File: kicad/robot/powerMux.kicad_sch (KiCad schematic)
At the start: 8 parts, among them Q1 Q_NMOS_GDS, U4 NCP3901

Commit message: Assigned resistor footprints
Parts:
- R16, R17, R18: footprint (none) -> Resistor_SMD:R_0603_1608Metric
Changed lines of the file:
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@@
       (effects (font (size 1.27 1.27)) (justify left))
     )
-    (property "Footprint" "" (id 2) (at 172.212 123.19 90)
+    (property "Footprint" "Resistor_SMD:R_0603_1608Metric" (id 2) (at 172.212 123.19 90)
       (effects (font (size 1.27 1.27)) hide)
     )
@@
       (effects (font (size 1.27 1.27)) (justify left))
     )
-    (property "Footprint" "" (id 2) (at 207.772 67.31 90)
+    (property "Footprint" "Resistor_SMD:R_0603_1608Metric" (id 2) (at 207.772 67.31 90)
       (effects (font (size 1.27 1.27)) hide)
     )
@@
       (effects (font (size 1.27 1.27)) (justify left))
     )
-    (property "Footprint" "" (id 2) (at 172.212 135.89 90)
+    (property "Footprint" "Resistor_SMD:R_0603_1608Metric" (id 2) (at 172.212 135.89 90)
       (effects (font (size 1.27 1.27)) hide)
     )

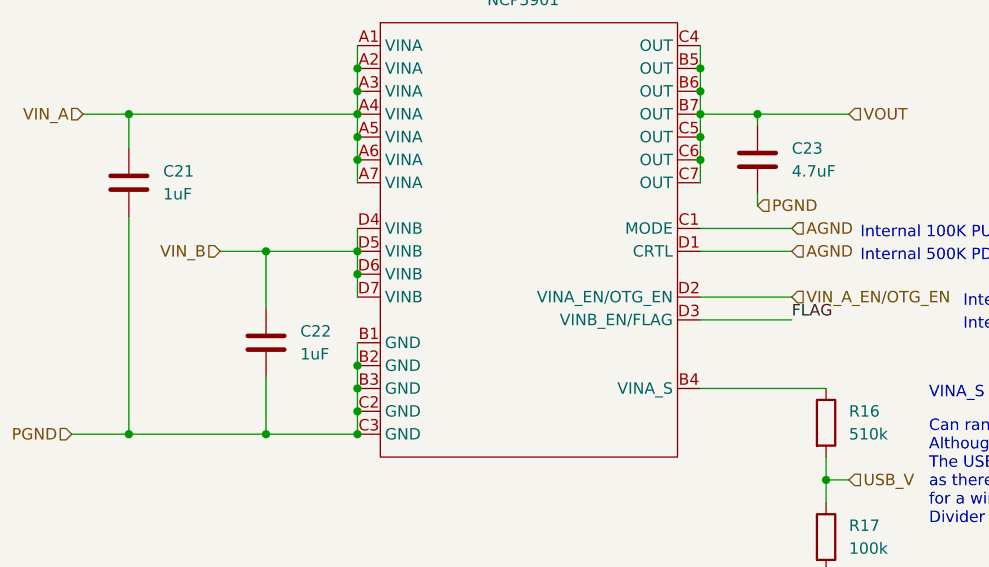
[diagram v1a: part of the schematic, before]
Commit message: Assigned capacitor footprints
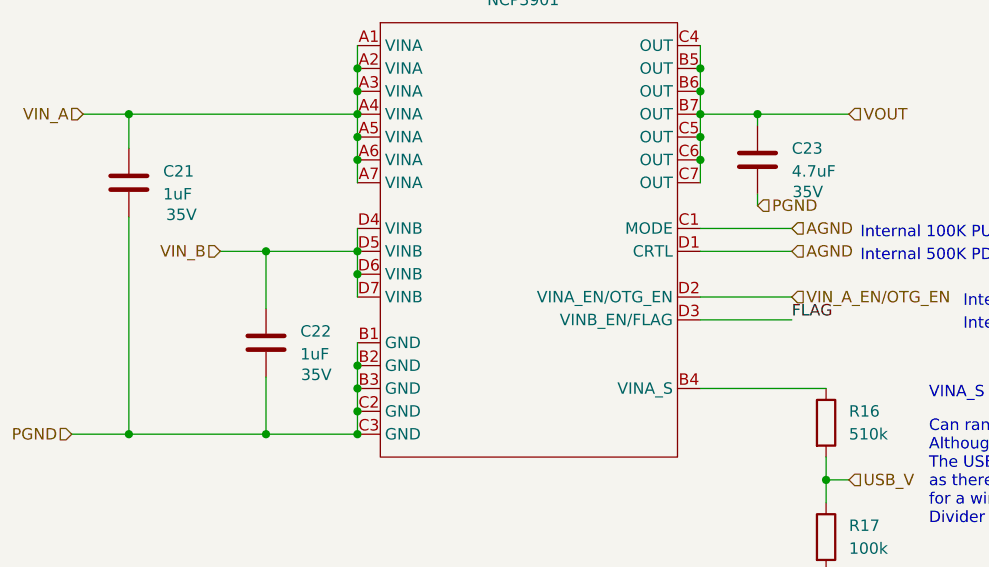
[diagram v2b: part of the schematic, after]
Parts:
- C21, C22, C23: footprint (none) -> Capacitor_SMD:C_0805_2012Metric
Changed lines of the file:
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@@
   )
   (symbol (lib_id "Device:C") (at 166.37 93.98 0) (unit 1)
-    (in_bom yes) (on_board yes) (fields_autoplaced)
+    (in_bom yes) (on_board yes)
     (property "Reference" "C23" (id 0) (at 170.18 92.7099 0)
       (effects (font (size 1.27 1.27)) (justify left))
@@
       (effects (font (size 1.27 1.27)) (justify left))
     )
-    (property "Footprint" "" (id 2) (at 167.3352 97.79 0)
+    (property "Footprint" "Capacitor_SMD:C_0805_2012Metric" (id 2) (at 167.3352 97.79 0)
       (effects (font (size 1.27 1.27)) hide)
     )
@@
       (effects (font (size 1.27 1.27)) hide)
     )
+    (property "Description" "35V" (id 4) (at 171.958 97.536 0))
     (pin "1")
     (pin "2")
@@
   )
   (symbol (lib_id "Device:C") (at 111.76 114.3 0) (unit 1)
-    (in_bom yes) (on_board yes) (fields_autoplaced)
+    (in_bom yes) (on_board yes)
     (property "Reference" "C22" (id 0) (at 115.57 113.0299 0)
       (effects (font (size 1.27 1.27)) (justify left))
@@
       (effects (font (size 1.27 1.27)) (justify left))
     )
-    (property "Footprint" "" (id 2) (at 112.7252 118.11 0)
+    (property "Footprint" "Capacitor_SMD:C_0805_2012Metric" (id 2) (at 112.7252 118.11 0)
       (effects (font (size 1.27 1.27)) hide)
     )
@@
       (effects (font (size 1.27 1.27)) hide)
     )
+    (property "Description" "35V" (id 4) (at 117.348 117.856 0))
     (pin "1")
     (pin "2")
@@
   )
   (symbol (lib_id "Device:C") (at 96.52 96.52 0) (unit 1)
-    (in_bom yes) (on_board yes) (fields_autoplaced)
+    (in_bom yes) (on_board yes)
     (property "Reference" "C21" (id 0) (at 100.33 95.2499 0)
       (effects (font (size 1.27 1.27)) (justify left))
@@
       (effects (font (size 1.27 1.27)) (justify left))
     )
-    (property "Footprint" "" (id 2) (at 97.4852 100.33 0)
+    (property "Footprint" "Capacitor_SMD:C_0805_2012Metric" (id 2) (at 97.4852 100.33 0)
       (effects (font (size 1.27 1.27)) hide)
     )
@@
       (effects (font (size 1.27 1.27)) hide)
     )
+    (property "Description" "35V" (id 4) (at 102.362 100.076 0))
     (pin "1")
     (pin "2")

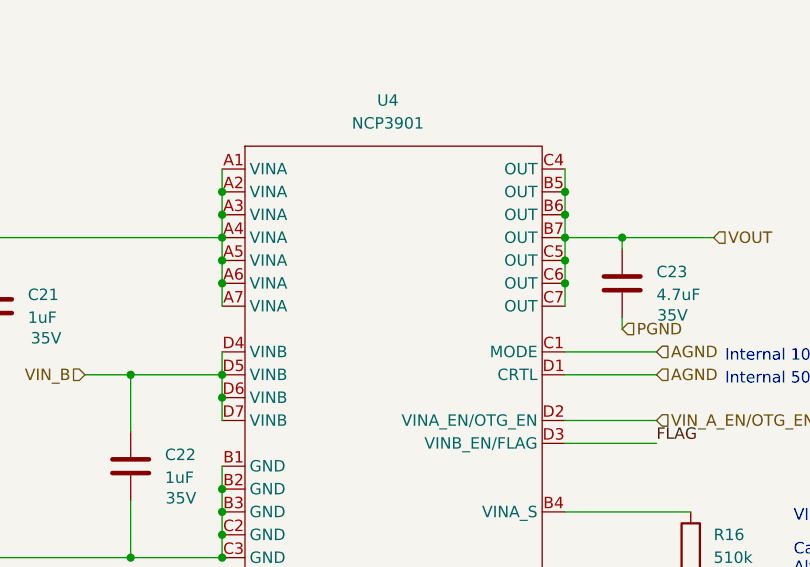
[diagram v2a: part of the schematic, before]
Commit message: Added footprint to NCP3901
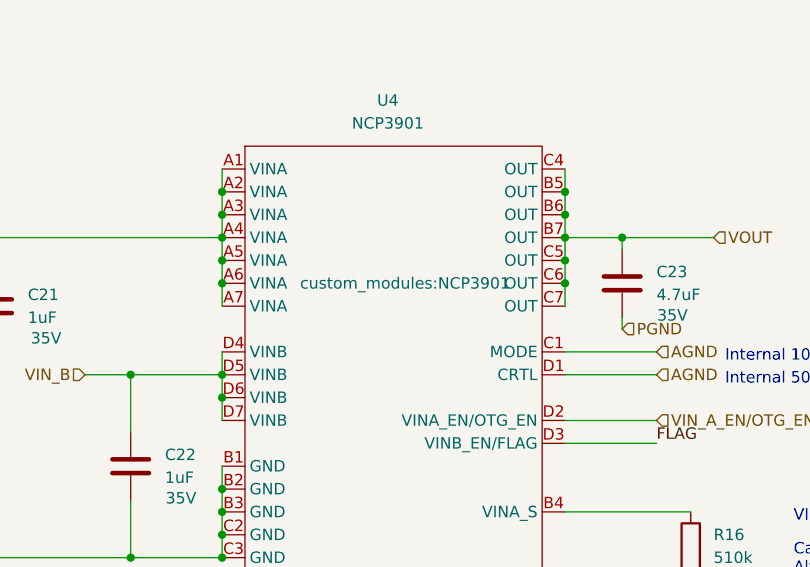
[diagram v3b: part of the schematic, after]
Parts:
- U4: footprint (none) -> custom_modules:NCP3901
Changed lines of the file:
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@@
     (property "Reference" "U4" (id 0) (at 140.335 73.66 0))
     (property "Value" "NCP3901" (id 1) (at 140.335 76.2 0))
-    (property "Footprint" "" (id 2) (at 142.24 93.98 0)
-      (effects (font (size 1.27 1.27)) hide)
-    )
+    (property "Footprint" "custom_modules:NCP3901" (id 2) (at 142.24 93.98 0))
     (property "Datasheet" "https://www.onsemi.com/pdf/datasheet/ncp3901-d.pdf" (id 3) (at 142.24 93.98 0)
       (effects (font (size 1.27 1.27)) hide)

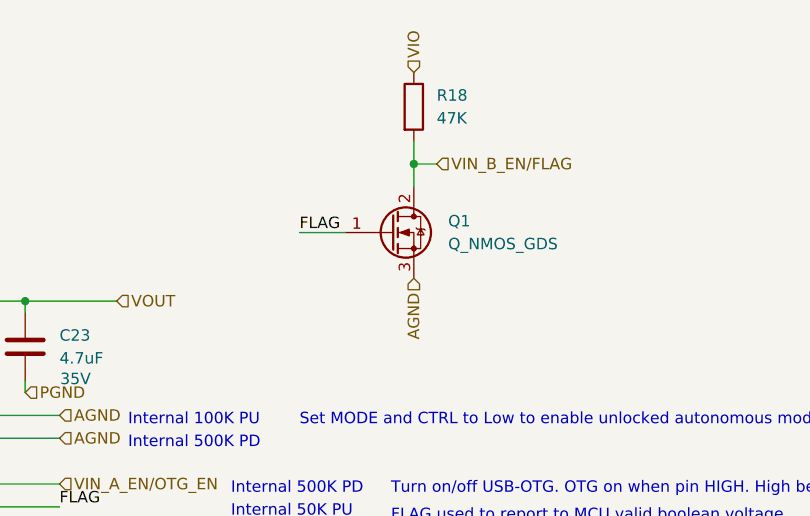
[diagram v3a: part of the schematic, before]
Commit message: Added part and footprint for mux mosfet.
Swapped pins 2 and 3 to match part.
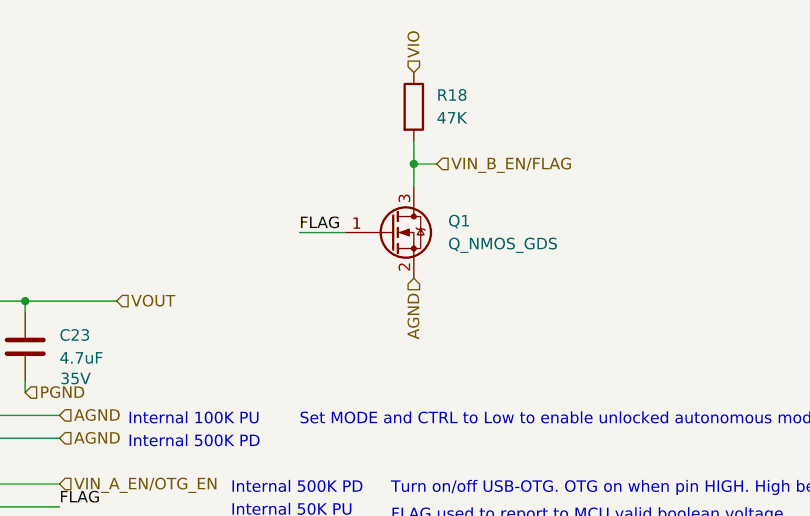
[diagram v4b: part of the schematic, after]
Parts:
- Q1: footprint (none) -> Package_TO_SOT_SMD:SOT-23; symbol Device:Q_NMOS_GDS -> Device:Q_NMOS_GSD; Part Number (none) -> T2N7002AK,LM
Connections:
- net AGND: now also Q1.2 (S); no longer Q1.3 (S)
- net VIN_B_EN/FLAG: now also Q1.3 (D); no longer Q1.2 (D)
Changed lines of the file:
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@@
     (pin "2")
   )
-  (symbol (lib_id "Device:Q_NMOS_GDS") (at 207.01 81.28 0) (unit 1)
+  (symbol (lib_id "Device:Q_NMOS_GSD") (at 207.01 81.28 0) (unit 1)
     (in_bom yes) (on_board yes) (fields_autoplaced)
     (property "Reference" "Q1" (id 0) (at 213.36 80.0099 0)
@@
       (effects (font (size 1.27 1.27)) (justify left))
     )
-    (property "Footprint" "" (id 2) (at 212.09 78.74 0)
+    (property "Footprint" "Package_TO_SOT_SMD:SOT-23" (id 2) (at 212.09 78.74 0)
       (effects (font (size 1.27 1.27)) hide)
     )
@@
       (effects (font (size 1.27 1.27)) hide)
     )
+    (property "Part Number" "T2N7002AK,LM" (id 5) (at 207.01 81.28 0)
+      (effects (font (size 1.27 1.27)) hide)
+    )

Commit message: WARNING more BOM batch edits
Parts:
- U4: Part Number (none) -> NCP3901
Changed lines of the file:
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@@
+      (effects (font (size 1.27 1.27)) hide)
+    )
+    (property "Part Number" "NCP3901" (id 4) (at 142.24 101.6 0)
       (effects (font (size 1.27 1.27)) hide)
     )

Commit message: Added stock counts to parts I have
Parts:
- U4: Stock (none) -> 25
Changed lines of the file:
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@@
+      (effects (font (size 1.27 1.27)) hide)
+    )
+    (property "Stock" "25" (id 5) (at 142.24 101.6 0)
       (effects (font (size 1.27 1.27)) hide)
     )

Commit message: Batch BOM edits adding manufactuer and part numbers only
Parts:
- Q1: Manufacturer (none) -> Toshiba
- R16: Manufacturer (none) -> Stackpole Electronics; Part Number (none) -> RMCF0603JT510K
- R17: Manufacturer (none) -> Stackpole Electronics; Part Number (none) -> RMCF0603JG100K
- R18: Manufacturer (none) -> Stackpole Electronics; Part Number (none) -> RMCF0603JT47K0
- U4: Manufacturer (none) -> onsemi
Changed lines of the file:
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@@
+      (effects (font (size 1.27 1.27)) hide)
+    )
+    (property "Manufacturer" "Stackpole Electronics" (id 4) (at 173.99 123.19 0)
+      (effects (font (size 1.27 1.27)) hide)
+    )
+    (property "Part Number" "RMCF0603JT510K" (id 5) (at 173.99 123.19 0)
       (effects (font (size 1.27 1.27)) hide)
     )
@@
       (effects (font (size 1.27 1.27)) hide)
     )
+    (property "Manufacturer" "Toshiba" (id 6) (at 207.01 81.28 0)
+      (effects (font (size 1.27 1.27)) hide)
+    )
     (pin "1")
     (pin "2")
@@
       (effects (font (size 1.27 1.27)) hide)
     )
+    (property "Manufacturer" "Stackpole Electronics" (id 4) (at 209.55 67.31 0)
+      (effects (font (size 1.27 1.27)) hide)
+    )
+    (property "Part Number" "RMCF0603JT47K0" (id 5) (at 209.55 67.31 0)
+      (effects (font (size 1.27 1.27)) hide)
+    )
     (pin "1")
     (pin "2")
@@
     )
     (property "Stock" "25" (id 5) (at 142.24 101.6 0)
+      (effects (font (size 1.27 1.27)) hide)
+    )
+    (property "Manufacturer" "onsemi" (id 6) (at 142.24 101.6 0)
       (effects (font (size 1.27 1.27)) hide)
     )
@@
       (effects (font (size 1.27 1.27)) hide)
     )
+    (property "Manufacturer" "Stackpole Electronics" (id 4) (at 173.99 135.89 0)
+      (effects (font (size 1.27 1.27)) hide)
+    )
+    (property "Part Number" "RMCF0603JG100K" (id 5) (at 173.99 135.89 0)
+      (effects (font (size 1.27 1.27)) hide)
+    )

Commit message: bulk BOM edits. Mainly dealing with cap voltage ratings and part selection
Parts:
- C21, C22: Manufacturer (none) -> Taiyo Yuden; Part Number (none) -> GMK212BJ105KGHT
- C23: Manufacturer (none) -> Murata; Part Number (none) -> GRM219R6YA475MA73D
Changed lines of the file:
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@@
     )
     (property "Description" "35V" (id 4) (at 171.958 97.536 0))
+    (property "Manufacturer" "Murata" (id 5) (at 166.37 93.98 0)
+      (effects (font (size 1.27 1.27)) hide)
+    )
+    (property "Part Number" "GRM219R6YA475MA73D" (id 6) (at 166.37 93.98 0)
+      (effects (font (size 1.27 1.27)) hide)
+    )
     (pin "1")
     (pin "2")
@@
     )
     (property "Description" "35V" (id 4) (at 117.348 117.856 0))
+    (property "Manufacturer" "Taiyo Yuden" (id 5) (at 111.76 114.3 0)
+      (effects (font (size 1.27 1.27)) hide)
+    )
+    (property "Part Number" "GMK212BJ105KGHT" (id 6) (at 111.76 114.3 0)
+      (effects (font (size 1.27 1.27)) hide)
+    )
     (pin "1")
     (pin "2")
@@
     )
     (property "Description" "35V" (id 4) (at 102.362 100.076 0))
+    (property "Manufacturer" "Taiyo Yuden" (id 5) (at 96.52 96.52 0)
+      (effects (font (size 1.27 1.27)) hide)
+    )
+    (property "Part Number" "GMK212BJ105KGHT" (id 6) (at 96.52 96.52 0)
+      (effects (font (size 1.27 1.27)) hide)
+    )
     (pin "1")
     (pin "2")
